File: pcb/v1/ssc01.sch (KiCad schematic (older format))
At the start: 4 parts

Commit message: start wiring RAM and ROM
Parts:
- removed U?: AS6C4008, symbol ssc:AS6C4008
- added U?: 62256, symbol ssc:62256
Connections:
- net labels added: BANK0, BANK1, BANK2, MEM_SELECT
- net labels removed: A15
- wire segments 16 -> 71
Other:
- note added: "Address bus"
- note added: "Data bus"

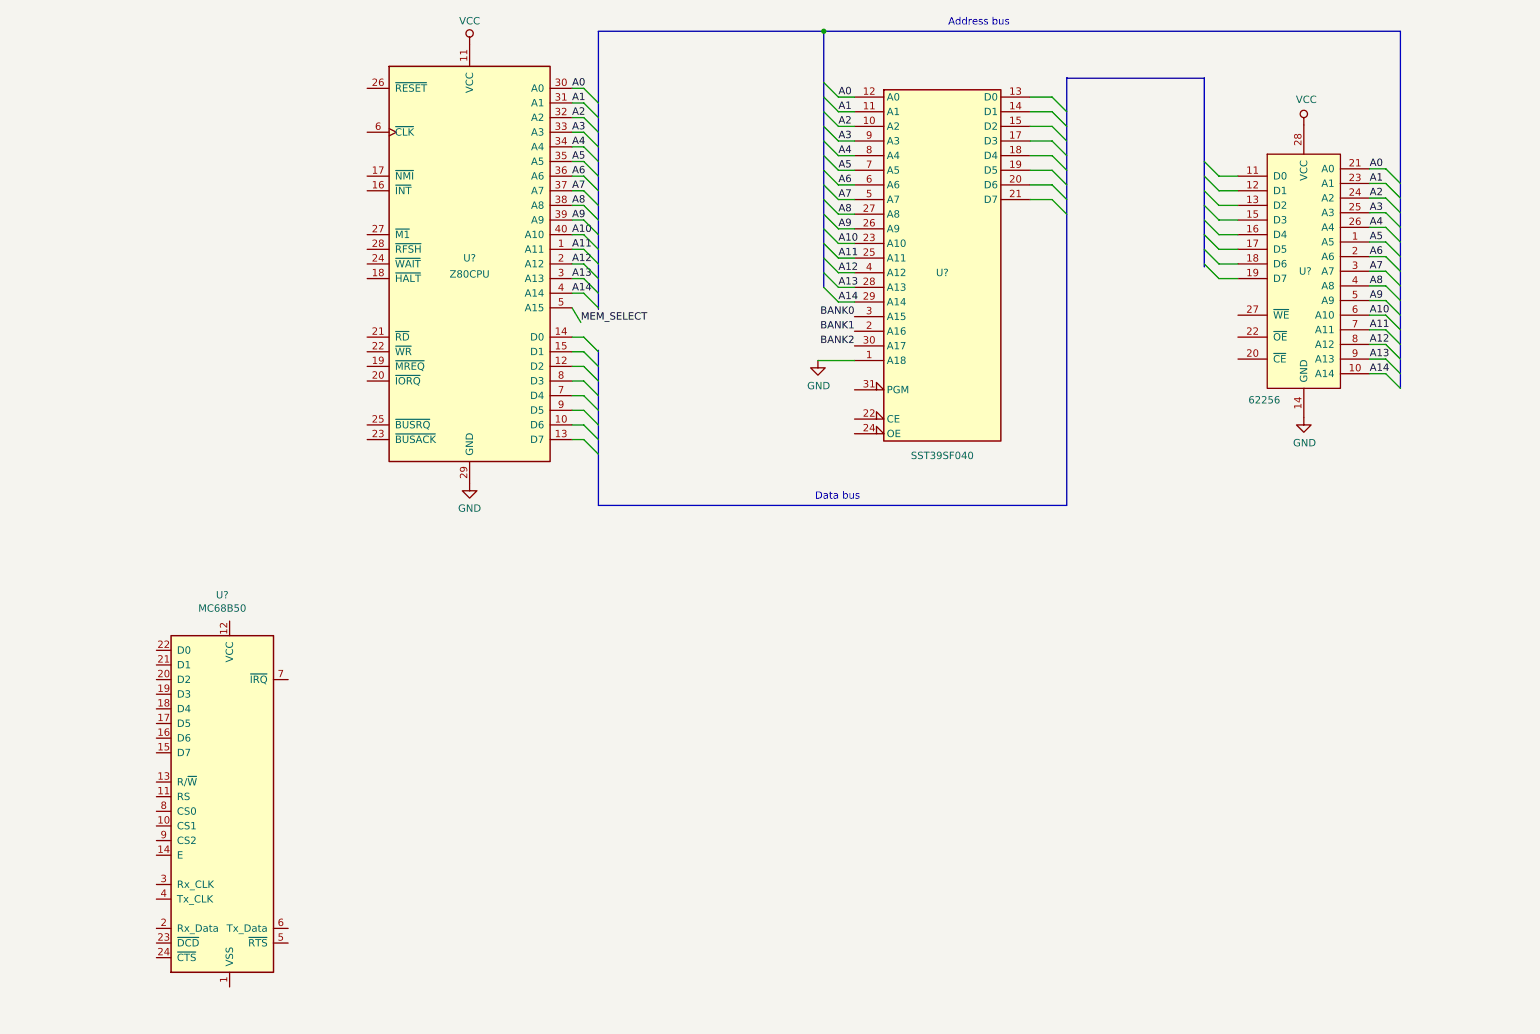
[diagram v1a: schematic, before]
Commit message: draw most of the schematic
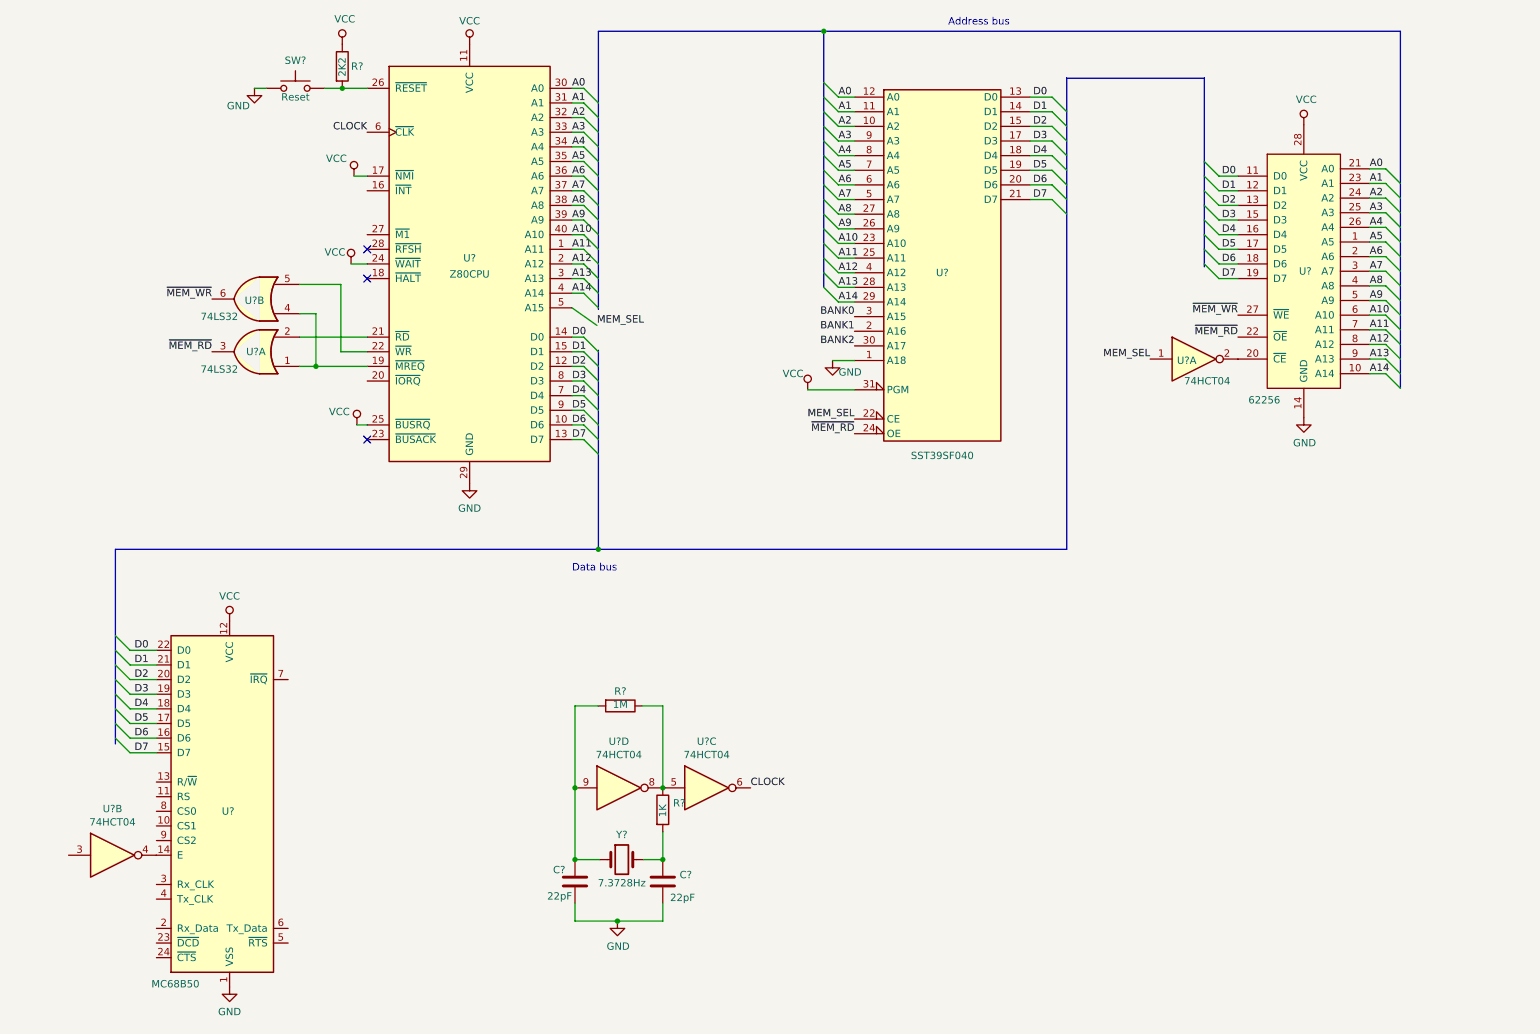
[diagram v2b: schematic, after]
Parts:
- added C? (x2): 22pF, symbol Device:C
- added R?: 1K, symbol Device:R
- added R?: 1M, symbol Device:R
- added R?: 2K2, symbol Device:R
- added SW?: Reset, symbol Switch:SW_Push
- added U? (x4): 74HCT04, symbol 74xx:74HCT04
- added U? (x2): 74LS32, symbol 74xx:74LS32
- added Y?: 7.3728Hz, symbol Device:Crystal
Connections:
- net MEM_SELECT is gone; now on net MEM_SEL: U?.5 (A15)
- net GND: now also U?.1 (VSS), C?.2, C?.2, SW?.1
- net VCC: now also U?.12 (VCC), U?.17 (~NMI~), U?.24 (~WAIT~), U?.25 (~BUSRQ~), U?.31 (PGM), R?.1
- net D6: now reaches U?.10 (D6)
- net D6: now also U?.16 (D6), U?.18 (D6), U?.20 (D6)
- net D2: now reaches U?.12 (D2)
- net D2: now also U?.13 (D2), U?.15 (D2), U?.20 (D2)
- net D7: now reaches U?.13 (D7)
- net D7: now also U?.15 (D7), U?.19 (D7), U?.21 (D7)
- net D0: now reaches U?.14 (D0)
- net D0: now also U?.11 (D0), U?.13 (D0), U?.22 (D0)
- net D1: now reaches U?.15 (D1)
- net D1: now also U?.12 (D1), U?.14 (D1), U?.21 (D1)
- net at U?.19 (~MREQ~): now also U?.1, U?.4
- net at U?.21 (~RD~): now also U?.2
- net at U?.22 (~WR~): now also U?.5
- net at U?.26 (~RESET~): now also R?.2, SW?.2
- net CLOCK: now reaches U?.6 (~CLK~)
- net CLOCK: now also U?.6
- net D4: now reaches U?.7 (D4)
- net D4: now also U?.16 (D4), U?.18 (D4), U?.18 (D4)
- net D3: now reaches U?.8 (D3)
- net D3: now also U?.15 (D3), U?.17 (D3), U?.19 (D3)
- net D5: now reaches U?.9 (D5)
- net D5: now also U?.17 (D5), U?.17 (D5), U?.19 (D5)
- net MEM_SEL: now reaches U?.22 (CE)
- net MEM_SEL: now also U?.1
- net ~MEM_RD: now reaches U?.24 (OE)
- net ~MEM_RD: now also U?.22 (~OE), U?.3
- net at U?.14 (E): now also U?.4
- net at U?.20 (~CE): now also U?.2
- net ~MEM_WR: now reaches U?.27 (~WE)
- net ~MEM_WR: now also U?.6
- new net: R?.1, R?.1, U?.5, U?.8
- new net: C?.1, R?.2, U?.9, Y?.1
- new net: C?.1, R?.2, Y?.2
- no-connect marks 0 -> 3

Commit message: finish first draft of a schematic
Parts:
- added J1: UART, symbol Connector_Generic:Conn_01x06
- added JP1: BANK0, symbol Device:Jumper_NC_Dual
- added JP2: BANK1, symbol Device:Jumper_NC_Dual
- added JP3: BANK2, symbol Device:Jumper_NC_Dual
- added R1: 3K3, symbol Device:R
- added R3, R4, R5: 2K7, symbol Device:R
- gave numbers to parts that had none: 13
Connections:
- net A0: now also U2.11 (RS)
- net A6: now also U2.9 (CS2)
- net A7: now also U2.10 (CS1)
- net BANK0: now also JP1.2
- net BANK1: now also JP2.2
- net BANK2: now also JP3.2
- net CLOCK: now also U2.3 (Rx_CLK), U2.4 (Tx_CLK)
- net GND: now also U2.23 (~DCD), U2.24 (~CTS), J1.6 (Pin_6), JP1.3, JP2.3, JP3.3
- net VCC: now also J1.4 (Pin_4), JP1.1, JP2.1, JP3.1, R1.1
- net ~INT: now reaches U4.16 (~INT~)
- net ~INT: now also U2.7 (~IRQ), R1.2
- net ~IORQ: now reaches U4.20 (~IORQ~)
- net ~IORQ: now also U1.3
- net ~WR: now reaches U3.5, U4.22 (~WR~)
- net ~WR: now also U2.13 (R/~W)
- net ~M1: now reaches U4.27 (~M1~)
- net ~M1: now also U2.8 (CS0)
- net RXD: now reaches U2.2 (Rx_Data)
- net RXD: now also R4.2
- net ~RTS: now reaches U2.5 (~RTS)
- net ~RTS: now also R5.2
- net TXD: now reaches U2.6 (Tx_Data)
- net TXD: now also R3.2
- new net: J1.2 (Pin_2), R3.1
- new net: J1.3 (Pin_3), R4.1
- new net: J1.5 (Pin_5), R5.1
- no-connect marks 3 -> 4
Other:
- moved on the sheet: C1, C2, R6, R7, U1C, U1D, Y1

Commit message: minor pcb changes
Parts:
- added JP4: BANK3, symbol Device:Jumper_NC_Dual
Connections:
- net GND: now also JP4.3; no longer U5.1 (A18)
- net VCC: now also JP4.1
- new net BANK3: JP4.2, U5.1 (A18)
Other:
- moved on the sheet: C1, C2, J1, JP1, JP2, JP3, R1, R2, R3, R4, R5, R6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

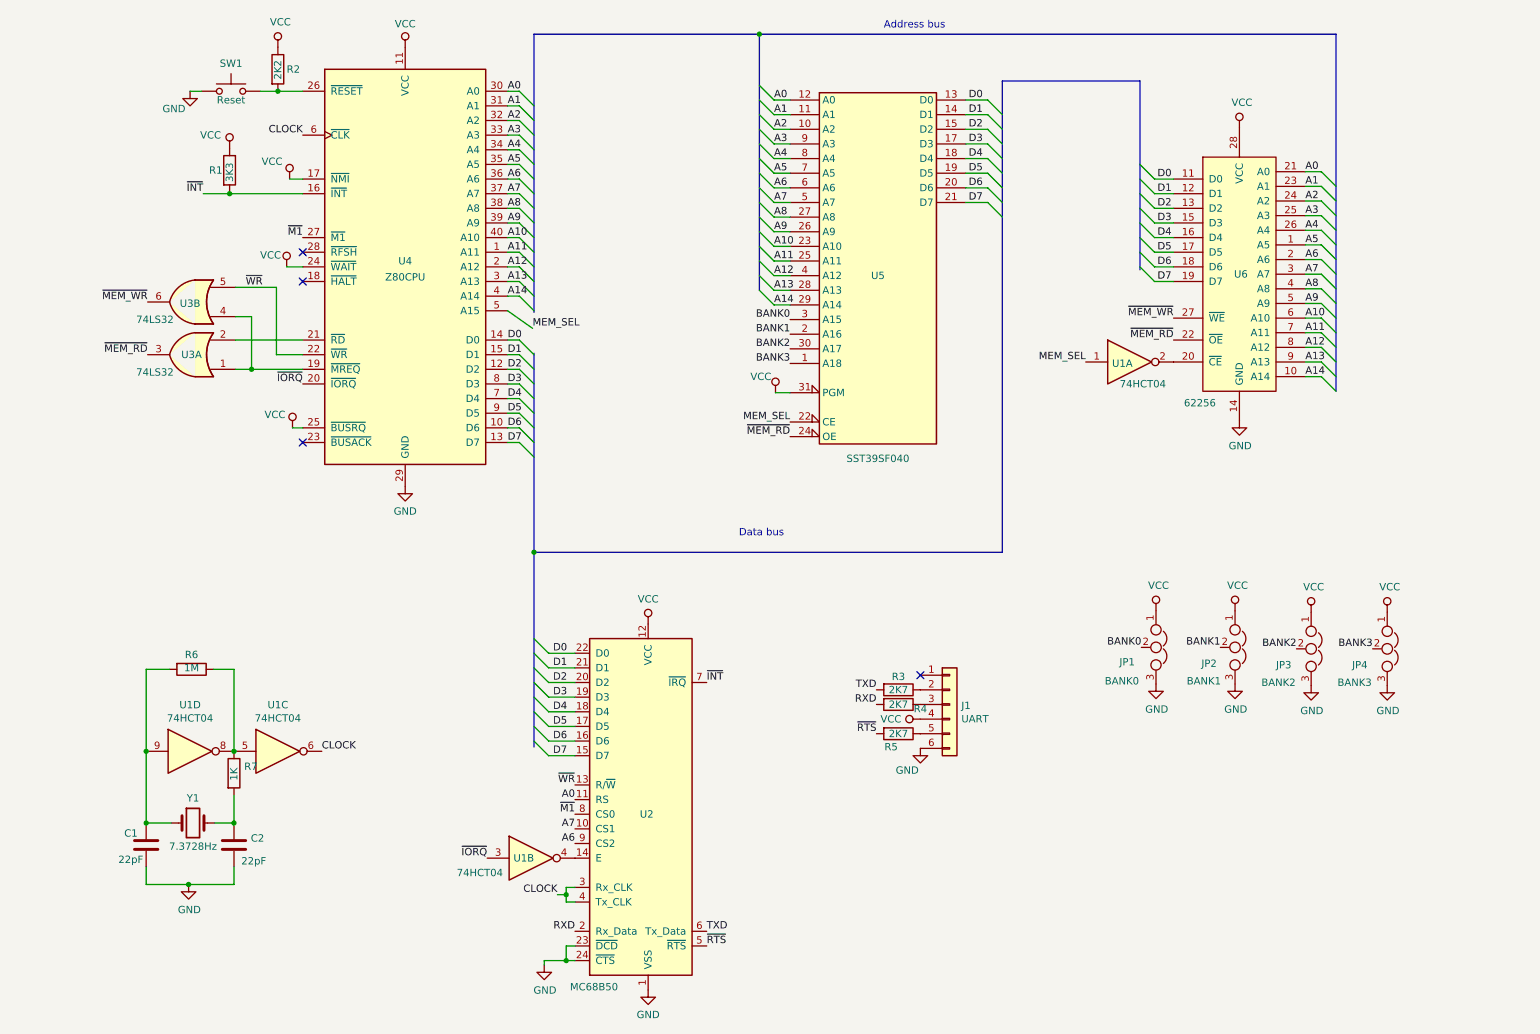
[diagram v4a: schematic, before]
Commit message: power and bypass caps
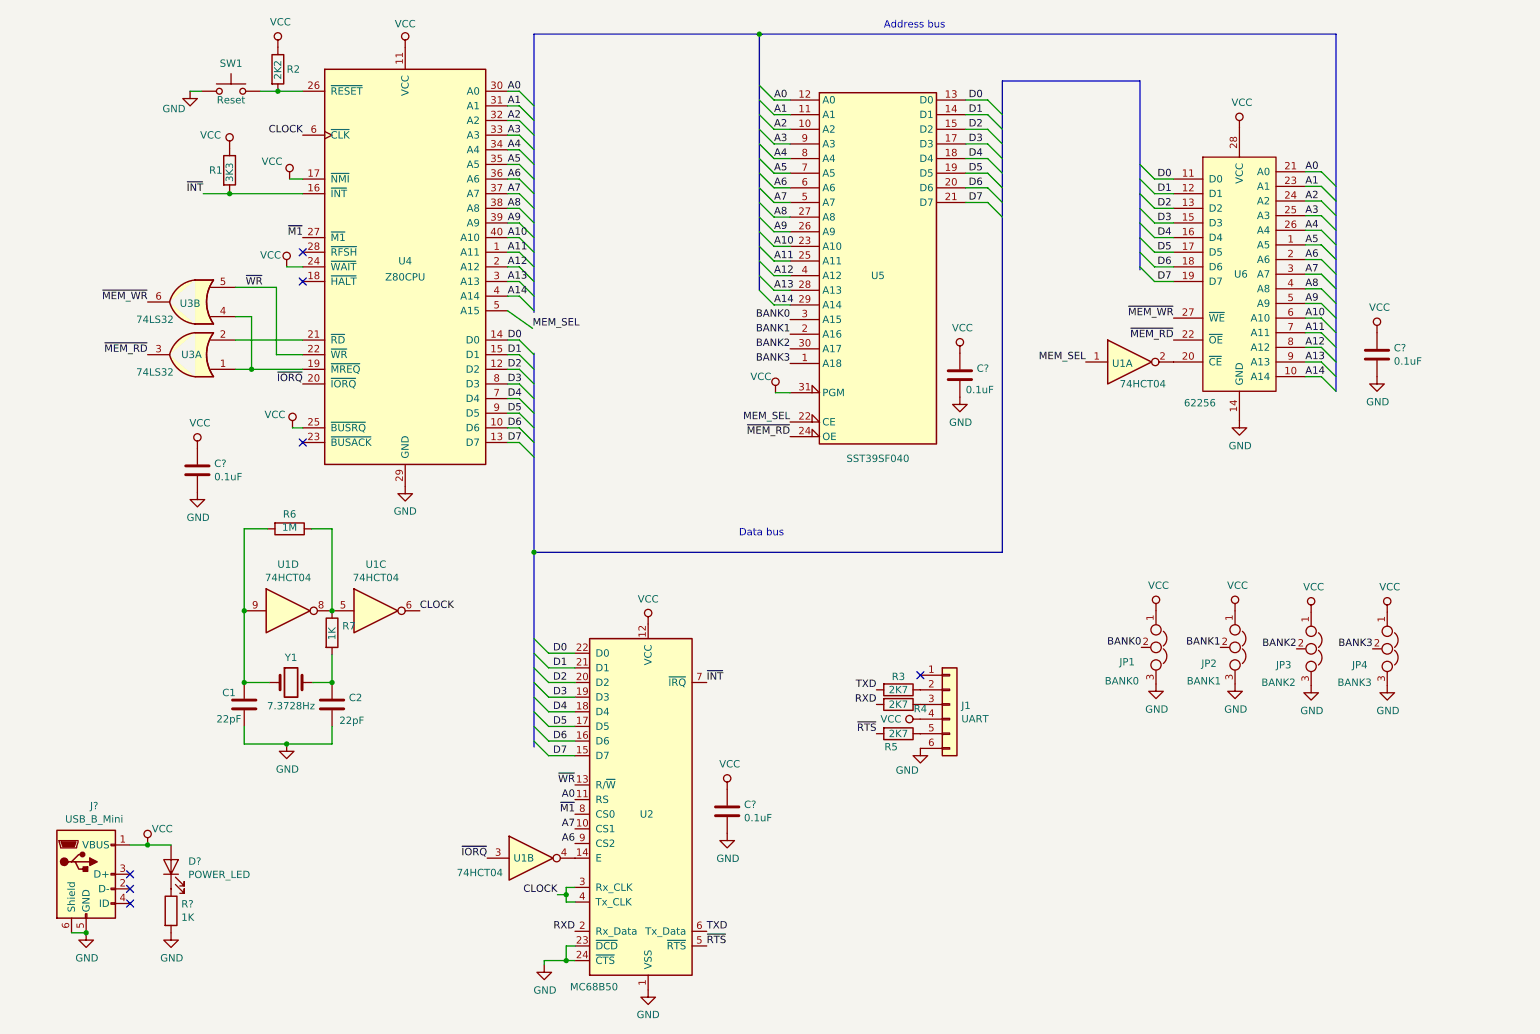
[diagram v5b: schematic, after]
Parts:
- added C? (x4): 0.1uF, symbol Device:C
- added D?: POWER_LED, symbol Device:LED
- added J?: USB_B_Mini, symbol Connector:USB_B_Mini
- added R?: 1K, symbol Device:R
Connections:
- net GND: now also C?.2, C?.2, C?.2, C?.2, J?.5 (GND), J?.6 (Shield), R?.2
- net VCC: now also C?.1, C?.1, C?.1, C?.1, D?.2 (A), J?.1 (VBUS)
- new net: D?.1 (K), R?.1
- no-connect marks 4 -> 7
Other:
- moved on the sheet: C1, C2, R6, R7, U1C, U1D, Y1

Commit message: minor pcb changes
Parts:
- removed JP4: BANK3, symbol Device:Jumper_NC_Dual
- added JP4: UART_VCC, symbol Device:Jumper_NO_Small
- gave numbers to parts that had none: 7
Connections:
- net BANK3 is gone; now on net GND: U5.1 (A18)
- net VCC: now also JP4.1; no longer J1.4 (Pin_4)
- new net: J1.4 (Pin_4), JP4.2
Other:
- moved on the sheet: C1, C2, C3, D1, J1, J2, JP1, JP2, JP3, R1, R2, R3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

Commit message: start the layout
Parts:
- added C7, C8: 0.1uF, Capacitor_THT:C_Disc_D3.8mm_W2.6mm_P2.50mm, symbol Device:C
- added unit 7 of U1
- added unit 5 of U3
- C1, C2, C3, C4, C5, C6: footprint (none) -> Capacitor_THT:C_Disc_D3.8mm_W2.6mm_P2.50mm
- D1: footprint (none) -> LED_THT:LED_D5.0mm
- J1: footprint (none) -> Connector_PinHeader_2.54mm:PinHeader_1x06_P2.54mm_Vertical
- J2: footprint (none) -> Connector_USB:USB_Mini-B_Lumberg_2486_01_Horizontal
- JP1, JP2, JP3: footprint (none) -> Connector_PinHeader_2.54mm:PinHeader_1x03_P2.54mm_Vertical
- JP4: footprint (none) -> Connector_PinHeader_2.54mm:PinHeader_1x02_P2.54mm_Vertical
- R1, R2, R3, R4, R5, R6, R7, R8: footprint (none) -> Resistor_THT:R_Axial_DIN0207_L6.3mm_D2.5mm_P10.16mm_Horizontal
- SW1: footprint (none) -> Button_Switch_THT:SW_PUSH_6mm
- U1, U3: footprint (none) -> Package_DIP:DIP-14_W7.62mm_LongPads
- U4: footprint (none) -> Package_DIP:DIP-40_W15.24mm_Socket_LongPads
- U5: footprint (none) -> Package_DIP:DIP-32_W15.24mm_LongPads
- U6: footprint (none) -> Package_DIP:DIP-28_W7.62mm_LongPads
- Y1: footprint (none) -> Crystal:Crystal_HC49-4H_Vertical
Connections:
- net GND: now also C7.2, C8.2, U1.7 (GND), U3.7 (GND)
- net VCC: now also C7.1, C8.1, U1.14 (VCC), U3.14 (VCC)

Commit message: continue layout
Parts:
- D1: footprint LED_THT:LED_D5.0mm -> LED_SMD:LED_1206_3216Metric
- U1, U3: footprint (none) -> Package_DIP:DIP-14_W7.62mm_LongPads
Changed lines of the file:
@@
 F 0 "D1" V 2238 5222 50  0000 R CNN
 F 1 "POWER_LED" V 2147 5222 50  0000 R CNN
-F 2 "LED_THT:LED_D5.0mm" H 2200 5340 50  0001 C CNN
+F 2 "LED_SMD:LED_1206_3216Metric" H 2200 5340 50  0001 C CNN
 F 3 "~" H 2200 5340 50  0001 C CNN
 	1    2200 5340
@@
 F 0 "U1" H 8920 5370 50  0000 L CNN
 F 1 "74HCT04" H 8830 5280 50  0000 L CNN
-F 2 "" H 9000 5340 50  0001 C CNN
+F 2 "Package_DIP:DIP-14_W7.62mm_LongPads" H 9000 5340 50  0001 C CNN
 F 3 "http://www.nxp.com/documents/data_sheet/74HC_HCT04.pdf" H 9000 5340 50  0001 C CNN
 	7    9000 5340
@@
 F 0 "U3" H 10240 5400 50  0000 L CNN
 F 1 "74LS32" H 10180 5310 50  0000 L CNN
-F 2 "" H 10300 5360 50  0001 C CNN
+F 2 "Package_DIP:DIP-14_W7.62mm_LongPads" H 10300 5360 50  0001 C CNN
 F 3 "http://www.ti.com/lit/gpn/sn74LS32" H 10300 5360 50  0001 C CNN
 	5    10300 5360
